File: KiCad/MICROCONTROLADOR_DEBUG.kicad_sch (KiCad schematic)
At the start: 2 parts

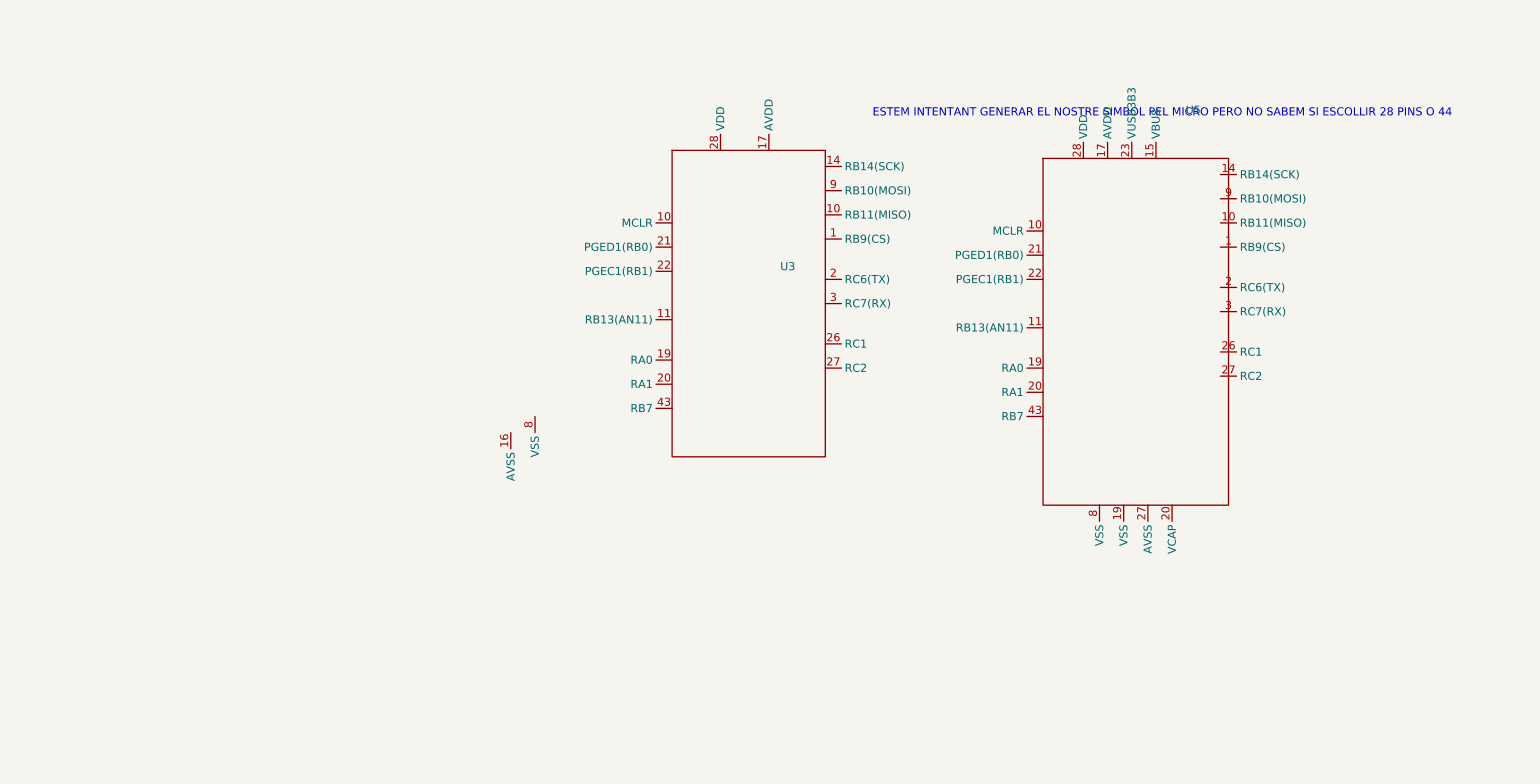
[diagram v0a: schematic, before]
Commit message: Actualizació final de les conexions del microcontrolador
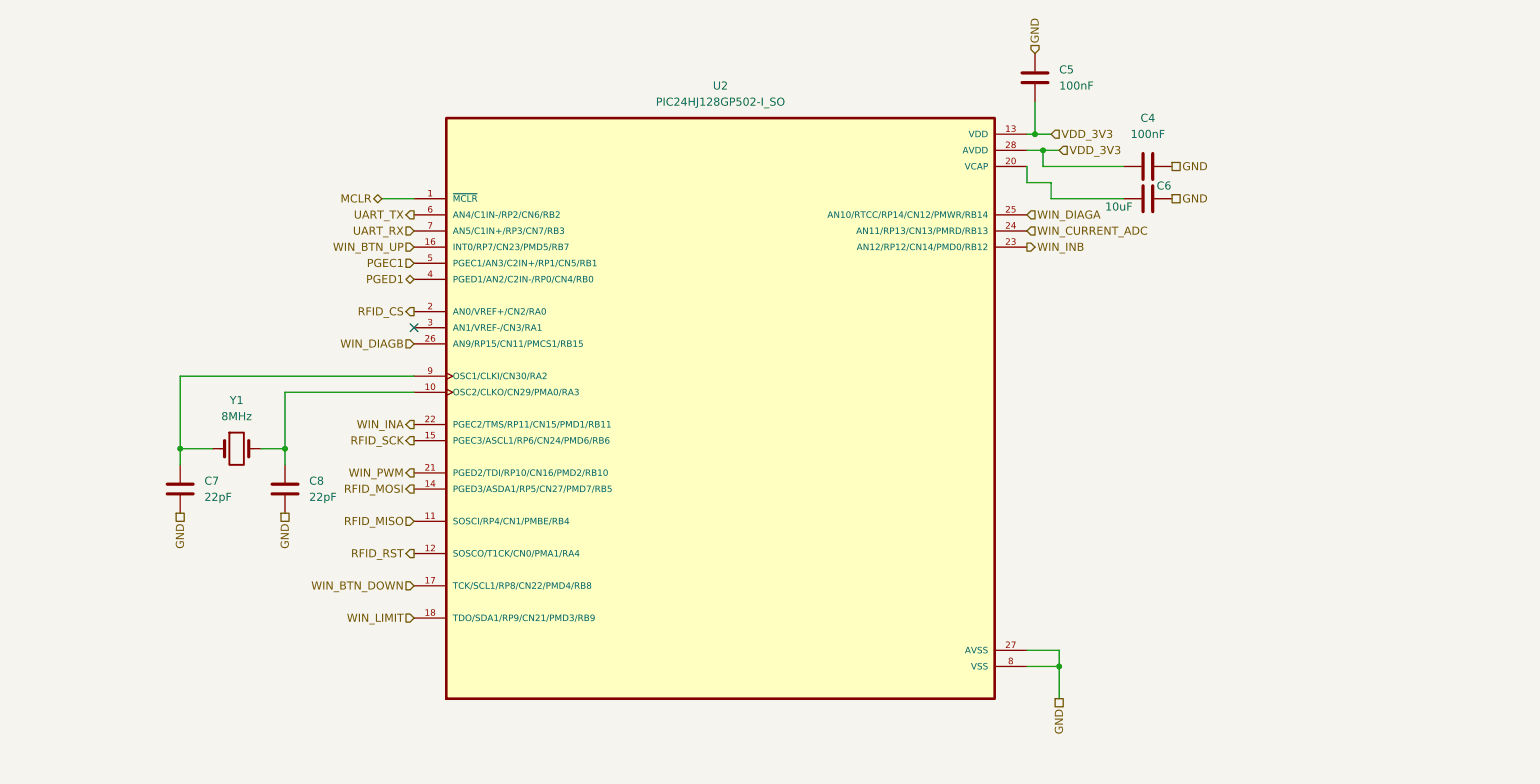
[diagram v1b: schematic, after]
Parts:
- removed U3, U5: ~, symbol PROJECTE:_1
- added C4, C5: 100nF, symbol Device:C
- added C6: 10uF, symbol Device:C
- added C7, C8: 22pF, symbol Device:C
- added U2: PIC24HJ128GP502-I_SO, PIC24HJ128GP502-I_SO:SOIC127P1030X265-28N, symbol PIC24HJ128GP502-I_SO:PIC24HJ128GP502-I_SO
- added Y1: 8MHz, symbol Device:Crystal
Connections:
- new net: C8.1, U2.10 (OSC2/CLKO/CN29/PMA0/RA3), Y1.2
- new net: C7.1, U2.9 (OSC1/CLKI/CN30/RA2), Y1.1
- new net: C6.1, U2.20 (VCAP)
- new net MCLR: U2.1 (~{MCLR})
- new net PGEC1: U2.5 (PGEC1/AN3/C2IN+/RP1/CN5/RB1)
- new net PGED1: U2.4 (PGED1/AN2/C2IN-/RP0/CN4/RB0)
- new net RFID_CS: U2.2 (AN0/VREF+/CN2/RA0)
- new net RFID_MISO: U2.11 (SOSCI/RP4/CN1/PMBE/RB4)
- new net RFID_MOSI: U2.14 (PGED3/ASDA1/RP5/CN27/PMD7/RB5)
- new net RFID_RST: U2.12 (SOSCO/T1CK/CN0/PMA1/RA4)
- new net RFID_SCK: U2.15 (PGEC3/ASCL1/RP6/CN24/PMD6/RB6)
- new net UART_RX: U2.7 (AN5/C1IN+/RP3/CN7/RB3)
- new net UART_TX: U2.6 (AN4/C1IN-/RP2/CN6/RB2)
- new net VDD_3V3: C4.1, C5.2, U2.13 (VDD), U2.28 (AVDD)
- new net VSS: C4.2, C5.1, C6.2, C7.2, C8.2, U2.19 (VSS), U2.27 (AVSS), U2.8 (VSS)
- new net WIN_BTN_DOWN: U2.17 (TCK/SCL1/RP8/CN22/PMD4/RB8)
- new net WIN_BTN_UP: U2.16 (INT0/RP7/CN23/PMD5/RB7)
- new net WIN_CURRENT_ADC: U2.24 (AN11/RP13/CN13/PMRD/RB13)
- new net WIN_DIAGA: U2.25 (AN10/RTCC/RP14/CN12/PMWR/RB14)
- new net WIN_DIAGB: U2.26 (AN9/RP15/CN11/PMCS1/RB15)
- new net WIN_INA: U2.22 (PGEC2/TMS/RP11/CN15/PMD1/RB11)
- new net WIN_INB: U2.23 (AN12/RP12/CN14/PMD0/RB12)
- new net WIN_LIMIT: U2.18 (TDO/SDA1/RP9/CN21/PMD3/RB9)
- new net WIN_PWM: U2.21 (PGED2/TDI/RP10/CN16/PMD2/RB10)
- no-connect marks 0 -> 1
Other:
- note removed: "ESTEM INTENTANT GENERAR EL NOSTRE SIMBOL PEL MICRO PERO NO SABEM SI ESCOLLIR 28 PINS O 44"

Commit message: Etiquetes de GND i VCC 3.3V canviades a simbols
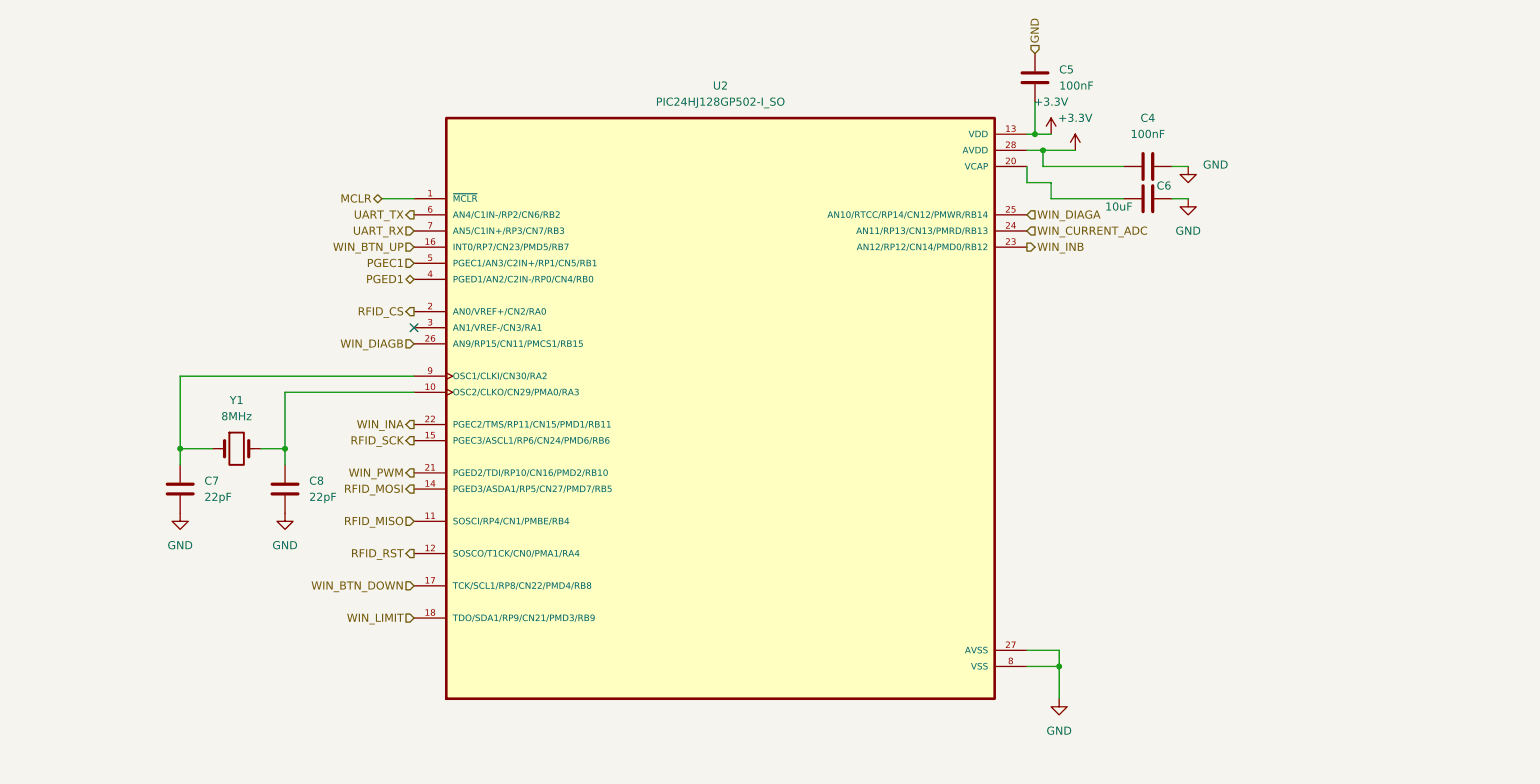
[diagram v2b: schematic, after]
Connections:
- net VDD_3V3 renamed +3.3V
- net VSS renamed GND

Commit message: Correció etapa d'alimentació e Inputs
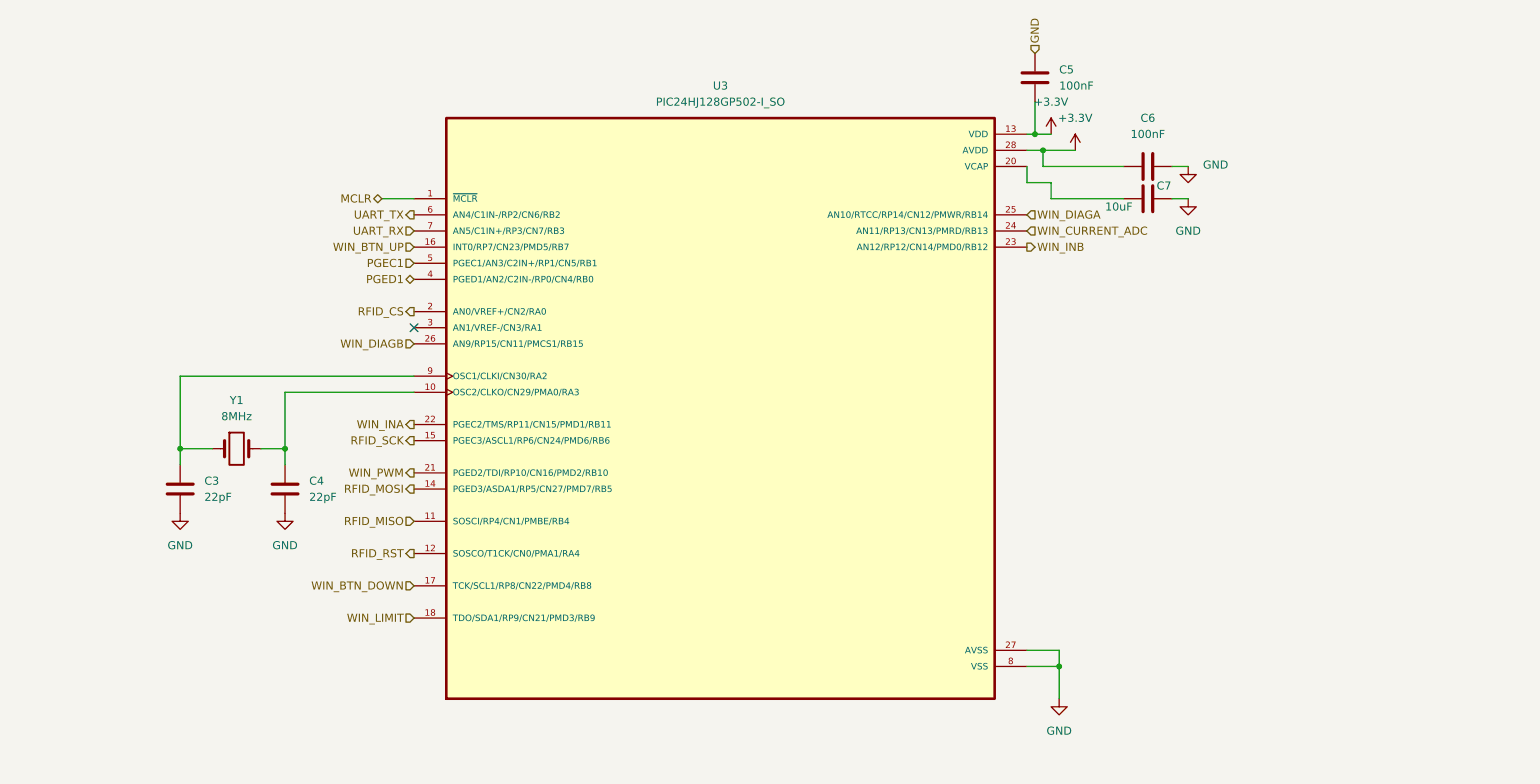
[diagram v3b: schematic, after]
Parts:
- renumbered C7 to C3, C8 to C4, C4 to C6, C6 to C7, U2 to U3
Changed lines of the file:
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@@
 		(dnp no)
 		(fields_autoplaced yes)
-		(property "Reference" "#PWR030"
+		(property "Reference" "#PWR011"
 			(at 203.2 43.18 0)
 			(effects
@@
 			(project ""
 				(path "/347831db-5db9-4aff-ad32-e56fd770e219/1f039355-d395-4709-b940-eff82ebe0f62"
-					(reference "#PWR030")
+					(reference "#PWR011")
 					(unit 1)
 				)
@@
 		(dnp no)
 		(fields_autoplaced yes)
-		(property "Reference" "C8"
+		(property "Reference" "C4"
 			(at 86.36 93.9799 0)
 			(effects
@@
 			(project "PROJECTE_EINES"
 				(path "/347831db-5db9-4aff-ad32-e56fd770e219/1f039355-d395-4709-b940-eff82ebe0f62"
-					(reference "C8")
+					(reference "C4")
 					(unit 1)
 				)
@@
 		(dnp no)
 		(fields_autoplaced yes)
-		(property "Reference" "#PWR032"
+		(property "Reference" "#PWR012"
 			(at 204.47 134.62 0)
 			(effects
@@
 			(project "PROJECTE_EINES"
 				(path "/347831db-5db9-4aff-ad32-e56fd770e219/1f039355-d395-4709-b940-eff82ebe0f62"
-					(reference "#PWR032")
+					(reference "#PWR012")
 					(unit 1)
 				)
@@
 		(on_board yes)
 		(dnp no)
-		(property "Reference" "C6"
+		(property "Reference" "C7"
 			(at 220.98 47.498 90)
 			(effects
@@
 			(project "PROJECTE_EINES"
 				(path "/347831db-5db9-4aff-ad32-e56fd770e219/1f039355-d395-4709-b940-eff82ebe0f62"
-					(reference "C6")
+					(reference "C7")
 					(unit 1)
 				)
@@
 		(on_board yes)
 		(dnp no)
-		(property "Reference" "#PWR029"
+		(property "Reference" "#PWR014"
 			(at 224.79 50.8 0)
 			(effects
@@
 			(project "PROJECTE_EINES"
 				(path "/347831db-5db9-4aff-ad32-e56fd770e219/1f039355-d395-4709-b940-eff82ebe0f62"
-					(reference "#PWR029")
+					(reference "#PWR014")
 					(unit 1)
 				)
@@
 		(dnp no)
 		(fields_autoplaced yes)
-		(property "Reference" "#PWR033"
+		(property "Reference" "#PWR09"
 			(at 66.04 105.41 0)
 			(effects
@@
 			(project "PROJECTE_EINES"
 				(path "/347831db-5db9-4aff-ad32-e56fd770e219/1f039355-d395-4709-b940-eff82ebe0f62"
-					(reference "#PWR033")
+					(reference "#PWR09")
 					(unit 1)
 				)
@@
 		(dnp no)
 		(fields_autoplaced yes)
-		(property "Reference" "#PWR028"
+		(property "Reference" "#PWR015"
 			(at 224.79 55.88 0)
 			(effects
@@
 			(project ""
 				(path "/347831db-5db9-4aff-ad32-e56fd770e219/1f039355-d395-4709-b940-eff82ebe0f62"
-					(reference "#PWR028")
+					(reference "#PWR015")
 					(unit 1)
 				)
@@
 		(dnp no)
 		(fields_autoplaced yes)
-		(property "Reference" "#PWR034"
+		(property "Reference" "#PWR010"
 			(at 82.55 105.41 0)
 			(effects
@@
 			(project "PROJECTE_EINES"
 				(path "/347831db-5db9-4aff-ad32-e56fd770e219/1f039355-d395-4709-b940-eff82ebe0f62"
-					(reference "#PWR034")
+					(reference "#PWR010")
 					(unit 1)
 				)
@@
 		(dnp no)
 		(fields_autoplaced yes)
-		(property "Reference" "C4"
+		(property "Reference" "C6"
 			(at 218.44 36.83 90)
 			(effects
@@
 			(project "PROJECTE_EINES"
 				(path "/347831db-5db9-4aff-ad32-e56fd770e219/1f039355-d395-4709-b940-eff82ebe0f62"
-					(reference "C4")
+					(reference "C6")
 					(unit 1)
 				)
@@
 		(dnp no)
 		(fields_autoplaced yes)
-		(property "Reference" "U2"
+		(property "Reference" "U3"
 			(at 151.13 31.75 0)
 			(effects
@@
 			(project ""
 				(path "/347831db-5db9-4aff-ad32-e56fd770e219/1f039355-d395-4709-b940-eff82ebe0f62"
-					(reference "U2")
+					(reference "U3")
 					(unit 1)
 				)
@@
 		(dnp no)
 		(fields_autoplaced yes)
-		(property "Reference" "C7"
+		(property "Reference" "C3"
 			(at 69.85 93.9799 0)
 			(effects
@@
 			(project ""
 				(path "/347831db-5db9-4aff-ad32-e56fd770e219/1f039355-d395-4709-b940-eff82ebe0f62"
-					(reference "C7")
+					(reference "C3")
 					(unit 1)
 				)
@@
 		(dnp no)
 		(fields_autoplaced yes)
-		(property "Reference" "#PWR031"
+		(property "Reference" "#PWR013"
 			(at 207.01 45.72 0)
 			(effects
@@
 			(project "PROJECTE_EINES"
 				(path "/347831db-5db9-4aff-ad32-e56fd770e219/1f039355-d395-4709-b940-eff82ebe0f62"
-					(reference "#PWR031")
-					(unit 1)
-				)
+					(reference "#PWR013")
+					(unit 1)
+				)

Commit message: Actualizació Footprints
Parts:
- Y1: footprint (none) -> Crystal:Crystal_SMD_3225-4Pin_3.2x2.5mm
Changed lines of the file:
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@@
 			)
 		)
-		(property "Footprint" ""
+		(property "Footprint" "Crystal:Crystal_SMD_3225-4Pin_3.2x2.5mm"
 			(at 74.93 88.9 0)
 			(effects
